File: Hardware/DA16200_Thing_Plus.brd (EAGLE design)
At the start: 22.9 x 59.7 mm, 131 parts, among them J2 THING_PLUS, J3 Qwiic, J5 USB C, J7 CORTEX_JTAG_DEBUG_PTH_NS, Q1 20V/4.2A/52mΩ/1.4W, U1 DA16200MOD, U2 CH340E_MSOP10, U3 MCP73831, U7 XC6222B331MR-G

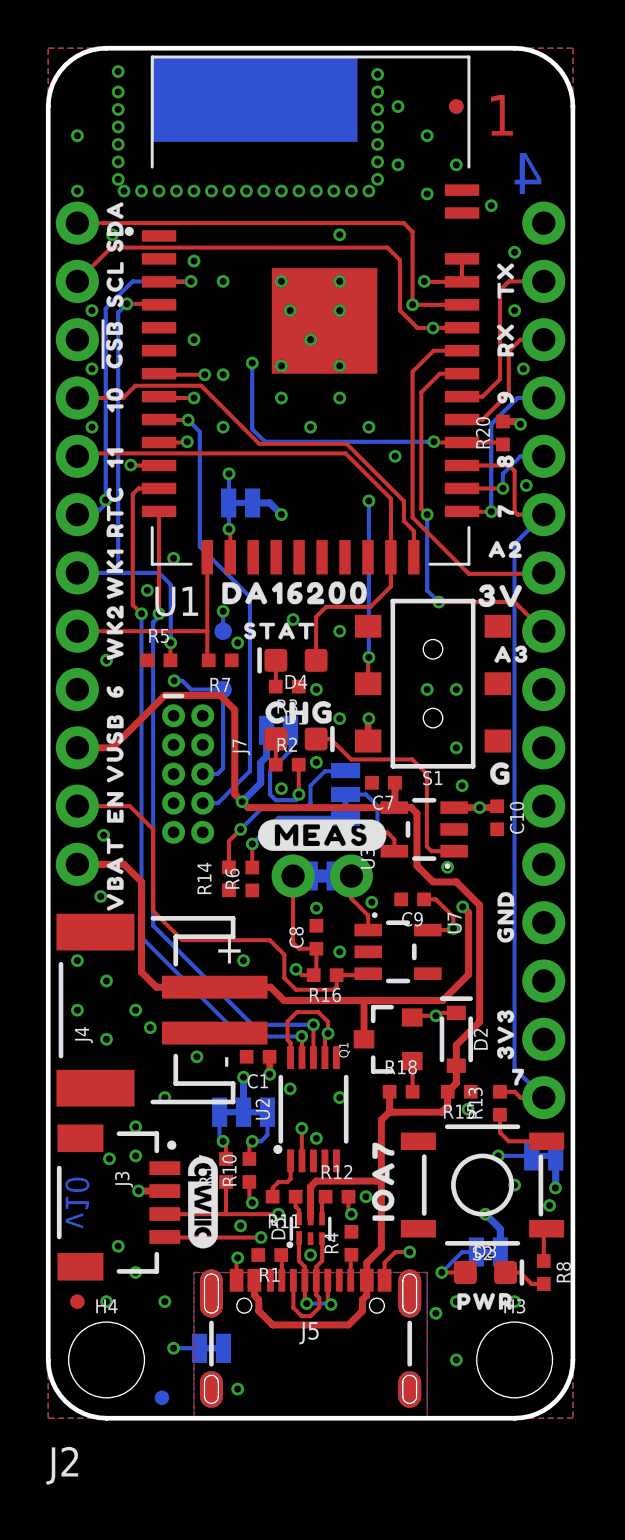
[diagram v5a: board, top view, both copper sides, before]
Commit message: Run through engineering checklist
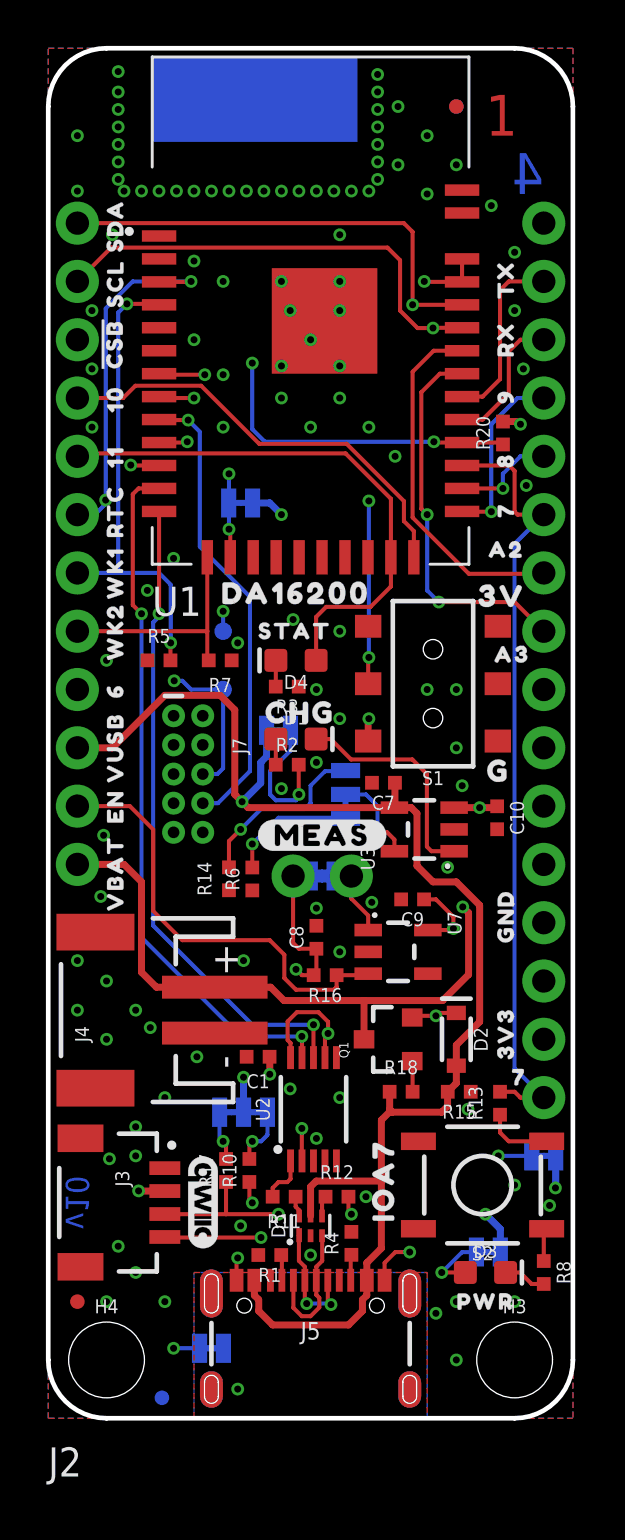
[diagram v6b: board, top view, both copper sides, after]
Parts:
- moved U$1 0.63 mm to (8.64, 34.3)
- moved U$4 0.18 mm to (18.4, 28.2)
- moved D5 0.13 mm to (11.4, 8.38)
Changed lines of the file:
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@@
 <?xml version="1.0" encoding="utf-8"?>
 <!DOCTYPE eagle SYSTEM "eagle.dtd">
-<eagle version="9.4.2">
+<eagle version="9.5.2">
 <drawing>
 <settings>
@@
 <layer number="38" name="bTest" color="7" fill="1" visible="no" active="yes"/>
 <layer number="39" name="tKeepout" color="4" fill="11" visible="yes" active="yes"/>
-<layer number="40" name="bKeepout" color="1" fill="11" visible="yes" active="yes"/>
+<layer number="40" name="bKeepout" color="1" fill="11" visible="no" active="yes"/>
 <layer number="41" name="tRestrict" color="4" fill="10" visible="no" active="yes"/>
 <layer number="42" name="bRestrict" color="1" fill="10" visible="no" active="yes"/>
@@
 <layer number="45" name="Holes" color="7" fill="1" visible="yes" active="yes"/>
 <layer number="46" name="Milling" color="3" fill="1" visible="no" active="yes"/>
-<layer number="47" name="Measures" color="7" fill="1" visible="no" active="yes"/>
+<layer number="47" name="Measures" color="7" fill="1" visible="yes" active="yes"/>
 <layer number="48" name="Document" color="7" fill="1" visible="no" active="yes"/>
 <layer number="49" name="Reference" color="7" fill="1" visible="no" active="yes"/>
@@
 <dimension x1="0" y1="0" x2="2.54" y2="2.54" x3="1.27" y3="-3.81" textsize="1.27" textratio="15" layer="47" dtype="horizontal" unit="inch"/>
 <dimension x1="0" y1="0" x2="2.54" y2="2.54" x3="-2.54" y3="1.27" textsize="1.27" textratio="15" layer="47" dtype="vertical" unit="inch"/>
-<text x="7.239" y="19.812" size="1.27" layer="21" font="vector" ratio="15">+</text>
+<text x="7.112" y="19.431" size="1.27" layer="21" font="vector" ratio="15">+</text>
 <text x="8.255" y="15.24" size="1.27" layer="21" font="vector" ratio="15" rot="R90">-</text>
 <text x="13.081" y="-19.177" size="1.778" layer="51" font="vector" ratio="15">Priyanka Makin</text>
@@
 <attribute name="VALUE" x="19.177" y="8.382" size="0.6096" layer="28" font="vector" ratio="20" rot="MR180" align="top-center"/>
 </element>
-<element name="D5" library="SparkFun-IC-Power" package="SOT886" value="PRTR5V0U2F" x="11.43" y="8.255" smashed="yes" rot="R90">
-<attribute name="NAME" x="10.33" y="8.255" size="0.6096" layer="25" ratio="20" rot="R90" align="bottom-center"/>
-<attribute name="PROD_ID" value="DIO-14084" x="11.43" y="8.255" size="1.778" layer="27" font="vector" ratio="15" rot="R90" display="off"/>
-<attribute name="VALUE" x="12.33" y="8.255" size="0.6096" layer="27" ratio="20" rot="R90" align="top-center"/>
+<element name="D5" library="SparkFun-IC-Power" package="SOT886" value="PRTR5V0U2F" x="11.43" y="8.382" smashed="yes" rot="R90">
+<attribute name="NAME" x="10.33" y="8.382" size="0.6096" layer="25" ratio="20" rot="R90" align="bottom-center"/>
+<attribute name="PROD_ID" value="DIO-14084" x="11.43" y="8.382" size="1.778" layer="27" font="vector" ratio="15" rot="R90" display="off"/>
+<attribute name="VALUE" x="12.33" y="8.382" size="0.6096" layer="27" ratio="20" rot="R90" align="top-center"/>
 </element>
 <element name="R11" library="SparkFun-Resistors" package="0402-TIGHT" value="27" x="10.279" y="9.652" smashed="yes" rot="R180">
@@
 <element name="U$84" library="output" package="#LED#0" value="" x="18.288" y="7.239" smashed="yes" rot="MR0"/>
 <element name="U$85" library="output" package="#SHLD#0" value="" x="13.208" y="2.921" smashed="yes" rot="MR0"/>
-<element name="U$1" library="output" package="STAT0" value="" x="8.001" y="34.29" smashed="yes"/>
+<element name="U$1" library="output" package="STAT0" value="" x="8.636" y="34.29" smashed="yes"/>
 <element name="U$2" library="output" package="CHG0" value="" x="8.763" y="30.734" smashed="yes"/>
 <element name="U$5" library="output" package="##RST##0" value="" x="21.209" y="13.97" smashed="yes" rot="MR0"/>
@@
 <attribute name="VALUE" x="16.764" y="35.814" size="0.6096" layer="27" font="vector" ratio="20" rot="R180" align="top-center"/>
 </element>
-<element name="U$4" library="output" package="G0" value="" x="18.542" y="28.067" smashed="yes"/>
+<element name="U$4" library="output" package="G0" value="" x="18.415" y="28.194" smashed="yes"/>
 <element name="U$9" library="output" package="3V0" value="" x="18.034" y="35.814" smashed="yes"/>
 <element name="CHG_LED" library="SparkFun-Jumpers" package="SMT-JUMPER_2_NC_TRACE_SILK" package3d_urn="urn:adsk.eagle:package:39281/1" value="JUMPER-SMT_2_NC_TRACE_SILK" x="10.033" y="29.972" smashed="yes" rot="MR0">
@@
 <wire x1="13.6902" y1="4.6732" x2="13.6902" y2="5.165875" width="0.3048" layer="1"/>
 <wire x1="11.6757875" y1="10.333" x2="11.43" y2="10.0872125" width="0.3048" layer="1"/>
-<wire x1="11.43" y1="8.685" x2="11.43" y2="10.0872125" width="0.3048" layer="1"/>
+<wire x1="11.43" y1="8.812" x2="11.43" y2="10.0872125" width="0.3048" layer="1"/>
 <wire x1="14.515" y1="10.333" x2="14.515" y2="7.407" width="0.3048" layer="1"/>
 <wire x1="14.515" y1="7.407" x2="13.88" y2="6.772" width="0.3048" layer="1"/>
@@
 <contactref element="R16" pad="2"/>
 <contactref element="C8" pad="1"/>
-<contactref element="MEAS" pad="3"/>
-<contactref element="MEAS" pad="1"/>
 <wire x1="11.565" y1="19.304" x2="11.684" y2="19.423" width="0.1778" layer="1"/>
 <wire x1="11.684" y1="19.423" x2="11.684" y2="20.455" width="0.1778" layer="1"/>
@@
 <wire x1="16.891" y1="18.549" x2="15.882" y2="19.558" width="0.1778" layer="15"/>
 <via x="16.891" y="17.533" extent="1-16" drill="0.3048"/>
+<contactref element="MEAS" pad="1"/>
+<contactref element="MEAS" pad="3"/>
+<wire x1="10.668" y1="20.709" x2="10.668" y2="23.622" width="0.1778" layer="1"/>
 <wire x1="11.43" y1="23.622" x2="10.668" y2="23.622" width="0.1778" layer="16"/>
-<wire x1="10.668" y1="20.709" x2="10.668" y2="23.622" width="0.1778" layer="1"/>
 </signal>
 <signal name="N$7">
@@
 <wire x1="11.18" y1="6.01" x2="11.18" y2="6.6" width="0.1778" layer="1"/>
 <wire x1="11.18" y1="6.6" x2="10.922" y2="6.858" width="0.1778" layer="1"/>
-<wire x1="10.922" y1="6.858" x2="10.922" y2="7.842" width="0.1778" layer="1"/>
-<wire x1="10.922" y1="7.842" x2="10.93" y2="7.85" width="0.1778" layer="1"/>
+<wire x1="10.922" y1="6.858" x2="10.922" y2="7.969" width="0.1778" layer="1"/>
+<wire x1="10.922" y1="7.969" x2="10.93" y2="7.977" width="0.1778" layer="1"/>
 </signal>
 <signal name="N$6">
@@
 <wire x1="11.68" y1="6.01" x2="11.68" y2="6.6" width="0.1778" layer="1"/>
 <wire x1="11.68" y1="6.6" x2="11.938" y2="6.858" width="0.1778" layer="1"/>
-<wire x1="11.938" y1="6.858" x2="11.938" y2="7.817" width="0.1778" layer="1"/>
-<wire x1="11.938" y1="7.817" x2="11.93" y2="7.825" width="0.1778" layer="1"/>
+<wire x1="11.938" y1="6.858" x2="11.938" y2="7.944" width="0.1778" layer="1"/>
+<wire x1="11.938" y1="7.944" x2="11.93" y2="7.952" width="0.1778" layer="1"/>
 </signal>
 <signal name="N$13">
 <contactref element="D5" pad="6"/>
 <contactref element="R11" pad="1"/>
-<wire x1="10.93" y1="8.685" x2="10.93" y2="9.066" width="0.1778" layer="1"/>
+<wire x1="10.93" y1="8.812" x2="10.93" y2="9.066" width="0.1778" layer="1"/>
 <wire x1="10.93" y1="9.066" x2="10.779" y2="9.217" width="0.1778" layer="1"/>
 <wire x1="10.779" y1="9.217" x2="10.779" y2="9.652" width="0.1778" layer="1"/>
@@
 <contactref element="D5" pad="4"/>
 <contactref element="R12" pad="1"/>
-<wire x1="11.93" y1="8.685" x2="11.93" y2="9.652" width="0.1778" layer="1"/>
+<wire x1="11.93" y1="8.812" x2="11.93" y2="9.652" width="0.1778" layer="1"/>
 <wire x1="12.081" y1="9.652" x2="11.93" y2="9.652" width="0.1778" layer="1"/>
 </signal>
